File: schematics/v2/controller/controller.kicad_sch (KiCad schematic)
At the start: 68 parts, among them J2 UART, J4 SPI1, J5 Power, J6 Ethernet, J7 Sensors, J8 SPI2, J9 SWD, SW1 BOOT0, SW2 RESET, U1 TPS2120, U2 TPS2120, U4 W5500, U5 AT25SF128A-SHB-T, U6 ADS131M02QPWRQ1, U7 SN74HC153DR, U8 SN74HC74D, U9 STM32G031K6Tx, Y1 KC2520Z, Y2 8.192MHz

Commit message: link controller module: version 1
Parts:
- removed C1, C3: 0.1uF, symbol Device:C_Small
- removed D1: LED, symbol Device:LED
- removed D2: Status, Diode_SMD:D_0603_1608Metric, symbol Device:LED
- removed J2: UART, symbol Connector:Conn_01x03_Pin
- removed J5: Power, symbol Connector:Conn_01x05_Pin
- removed J7: Sensors, symbol Connector:Conn_01x09_Pin
- removed J9: SWD, symbol Connector:Conn_01x05_Pin
- removed JP1: Default Clock Jumper, symbol Jumper:Jumper_3_Bridged12
- removed R10, R13, R4: 5k, symbol Device:R_Small_US
- removed R11: 270, Resistor_SMD:R_0603_1608Metric, symbol Device:R_Small_US
- removed R12, R3: 63.4k, symbol Device:R_Small_US
- removed R14, R5: 51.1K, symbol Device:R_Small_US
- removed R9: 23.7k, symbol Device:R_Small_US
- removed TP1: Vs1, symbol Connector:TestPoint
- removed TP2: Vs2, symbol Connector:TestPoint
- removed U1, U2: TPS2120, Link_Footprints:TPS2120, symbol Link_Components:TPS2120YFPR
- removed U7: SN74HC153DR, D16, symbol Link_Components:SN74HC153D
- removed U8: SN74HC74D, D14, symbol Link_Components:SN74HC74D
- added C22, C23: 10uF, Capacitor_SMD:C_0402_1005Metric, symbol Device:C_Small
- added C24, C25, C26: 0.1u, Capacitor_SMD:C_0402_1005Metric, symbol Device:C_Small
- added D4: LED2, Diode_SMD:D_0603_1608Metric, symbol Device:LED
- added D5: Power, Diode_SMD:D_0603_1608Metric, symbol Device:LED
- added FB2: FerriteBead_Small, Capacitor_SMD:C_0805_2012Metric, symbol Device:FerriteBead_Small
- added J1: Ethernet, Connector_PinHeader_2.54mm:PinHeader_1x06_P2.54mm_Vertical, symbol Connector:Conn_01x06_Pin
- added J3: Conn_ST_STDC14, Link_Footprints:FTSH_107_01_L_DV_K, symbol Connector:Conn_ST_STDC14
- added J8: Power, Connector_PinHeader_2.54mm:PinHeader_1x03_P2.54mm_Vertical, symbol Connector:Conn_01x03_Pin
- added R16, R17: 270, Resistor_SMD:R_0402_1005Metric, symbol Device:R_Small_US
- C1: renamed from C26; footprint (none) -> Capacitor_SMD:C_0402_1005Metric
- C10: renamed from C4; footprint (none) -> Capacitor_SMD:C_0402_1005Metric
- C11: renamed from C5; value 100nF -> 0.1uF; footprint (none) -> Capacitor_SMD:C_0402_1005Metric
- C12: renamed from C6; footprint (none) -> Capacitor_SMD:C_0402_1005Metric
- C13: renamed from C7; footprint (none) -> Capacitor_SMD:C_0402_1005Metric
- C14: renamed from C8; footprint (none) -> Capacitor_SMD:C_0402_1005Metric
- C15: renamed from C9; footprint (none) -> Capacitor_SMD:C_0402_1005Metric
- C16: renamed from C10; footprint (none) -> Capacitor_SMD:C_0402_1005Metric
- C17: renamed from C11; footprint (none) -> Capacitor_SMD:C_0402_1005Metric
- C18: renamed from C12; footprint (none) -> Capacitor_SMD:C_0402_1005Metric
- C19: renamed from C13; footprint (none) -> Capacitor_SMD:C_0402_1005Metric
- C2: renamed from C27; footprint (none) -> Capacitor_SMD:C_0402_1005Metric
- C20: renamed from C14; footprint (none) -> Capacitor_SMD:C_0402_1005Metric
- C21: renamed from C15; footprint (none) -> Capacitor_SMD:C_0402_1005Metric
- C3: renamed from C21; footprint (none) -> Capacitor_SMD:C_0402_1005Metric
- C4: renamed from C22; footprint (none) -> Capacitor_SMD:C_0402_1005Metric
- C5: renamed from C23; footprint (none) -> Capacitor_SMD:C_0402_1005Metric
- C6: renamed from C24; footprint (none) -> Capacitor_SMD:C_0402_1005Metric
- C8: renamed from C25; footprint (none) -> Capacitor_SMD:C_0402_1005Metric
- C9: renamed from C2; value 100n -> 0.1uF; footprint Capacitor_SMD:C_0603_1608Metric -> Capacitor_SMD:C_0402_1005Metric
- D3: value LED -> LED1; footprint (none) -> Diode_SMD:D_0603_1608Metric; LCSC (none) -> C2288; MPN (none) -> KT-0603B
- FB1: footprint (none) -> Capacitor_SMD:C_0805_2012Metric
- J4: footprint (none) -> Connector_PinHeader_2.54mm:PinHeader_1x05_P2.54mm_Vertical
- J5: renamed from J8; footprint (none) -> Connector_PinHeader_2.54mm:PinHeader_1x06_P2.54mm_Vertical
- J6: value Ethernet -> Sensors; footprint (none) -> Connector_PinHeader_2.54mm:PinHeader_1x08_P2.54mm_Vertical
- R1: value 23.7k -> 10k; footprint (none) -> Resistor_SMD:R_0402_1005Metric
- R11: renamed from R6; footprint Resistor_SMD:R_0603_1608Metric -> Resistor_SMD:R_0402_1005Metric
- R12: renamed from R8; footprint Resistor_SMD:R_0603_1608Metric -> Resistor_SMD:R_0402_1005Metric
- R14: renamed from R16; footprint (none) -> Resistor_SMD:R_0402_1005Metric
- R15: footprint (none) -> Resistor_SMD:R_0402_1005Metric; LCSC (none) -> C22369858; MPN (none) -> RCA03270RFLF
- R2: value 5k -> 10k; footprint (none) -> Resistor_SMD:R_0402_1005Metric
- R3: renamed from R17; footprint (none) -> Resistor_SMD:R_0402_1005Metric
- R4: renamed from R18; footprint (none) -> Resistor_SMD:R_0402_1005Metric
- R5: renamed from R20; footprint (none) -> Resistor_SMD:R_0402_1005Metric
- R6: renamed from R19; footprint (none) -> Resistor_SMD:R_0402_1005Metric
- R7: value 270 -> 10k; footprint (none) -> Resistor_SMD:R_0402_1005Metric
- U4: renamed from U6; footprint TSSOP20_PW_TEX -> Link_Footprints:ADS131M02-Q1
- U6: renamed from U5; footprint IC8_AT25SF128A-SHB-T_ADO -> Link_Footprints:AT25SF128A-SHB-T
- renumbered U9 to U5, U4 to U7, Y2 to Y1, Y1 to Y2
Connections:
- net ADS_Clock is gone; now on net PLL_Clock: U4.17 (CLKIN)
- net PS_Sel1 is gone; now on net W5500_NSS: U5.15 (PB0)
- net PS_Sel2 is gone; now on net LED1: U5.16 (PB1)
- net +3V3A: now also FB2.2; no longer FB1.2, U4.1 (AVDD)
- net +3V3D: now also R1.1, R2.1, R7.1, C22.2, C23.1, C24.2, C25.2, C26.2, FB2.1, J3.3 (VCC), J8.1 (Pin_1), J8.3 (Pin_3), R17.1; no longer C3.1, C4.1
- net 8.192MHz: now also U5.2 (PC14)
- net ACTLED: now also J1.6 (Pin_6); no longer J6.8 (Pin_8)
- net GND: now also J6.8 (Pin_8), C22.1, C23.2, C24.1, C25.1, C26.1, D4.1 (K), D5.1 (K), J3.11 (GNDDetect), J3.5 (GND), J3.7 (GND), J8.2 (Pin_2); no longer R2.1
- net LINKLED: now also J1.5 (Pin_5); no longer J6.7 (Pin_7)
- net N_RST: now also J3.12 (~{RST})
- net RX+: now also J1.4 (Pin_4); no longer J6.4 (Pin_4)
- net RX-: now also J1.3 (Pin_3); no longer J6.5 (Pin_5)
- net S1+: now also J6.5 (Pin_5)
- net S1-: now also J6.4 (Pin_4)
- net S2+: now also J6.1 (Pin_1), R6.1; no longer R5.1
- net S2-: now also J6.2 (Pin_2), R5.1; no longer R6.1
- net SDI: now also J6.7 (Pin_7), U5.18 (PA8); no longer U5.3 (PC15)
- net SPI1_MISO: now also U5.22 (PA11[PA9]); no longer U5.13 (PA6)
- net SPI1_MOSI: now also U5.23 (PA12[PA10]); no longer U5.14 (PA7)
- net SPI1_SCK: now also U5.27 (PB3); no longer U5.12 (PA5)
- net SPI2_MISO: now also J5.4 (Pin_4), U5.10 (PA3); no longer J5.3 (Pin_3), U5.30 (PB6)
- net SPI2_MOSI: now also J5.3 (Pin_3), U5.11 (PA4); no longer J5.2 (Pin_2), U5.31 (PB7)
- net SPI2_SCK: now also J5.2 (Pin_2), U5.7 (PA0); no longer J5.4 (Pin_4), U5.32 (PB8)
- net SWDIO: now also J3.4 (JTMS/SWDIO)
- net TX+: now also J1.2 (Pin_2); no longer J6.1 (Pin_1)
- net TX-: now also J1.1 (Pin_1); no longer J6.2 (Pin_2)
- net UART_RX: now also U5.31 (PB7), J3.13 (VCP_RX); no longer U5.10 (PA3)
- net UART_TX: now also U5.30 (PB6), J3.14 (VCP_TX); no longer U5.9 (PA2)
- net W5500_INTn: now also U5.13 (PA6); no longer U5.17 (PB2)
- net W5500_RST: now also U5.12 (PA5); no longer U5.27 (PB3)
- net MEM_NSS: now reaches R2.2
- net MEM_NSS: now also J5.6 (Pin_6), U5.14 (PA7), U6.1 (CS); no longer R1.1
- net LED1: now reaches R15.1
- net W5500_NSS: now reaches R7.2
- net W5500_NSS: now also J5.5 (Pin_5), U7.32 (~{SCS})
- net PLL_Clock: now reaches U5.19 (PA9)
- net +5V renamed ADC_NSS
- net ADC_NSS: now also J4.5 (Pin_5), U4.12 (CS), U5.26 (PA15)
- net ADS_ClockSelA renamed ADC_DRDY
- net ADC_DRDY: now also U4.13 (DRDY)
- net ADS_ClockSelB renamed ADC_RST
- net ADC_RST: now also U4.11 (*SYNC/RESET)
- removed net ADS_DRDY: U4.13 (DRDY), U5.26 (PA15)
- removed net ADS_RST: U4.11 (*SYNC/RESET), U5.23 (PA10/PA12)
- net BOOT0/SWCLK renamed BOOT0
- net BOOT0: now also J3.6 (JCLK/SWCLK)
- removed net SPI1_CS: J4.5 (Pin_5), U4.12 (CS), U5.11 (PA4)
- removed net SPI2_CS1: J5.6 (Pin_6), U5.18 (PA8), U7.32 (~{SCS})
- removed net SPI2_CS2: J5.5 (Pin_5), U5.22 (PA9/PA11), U6.1 (CS)
- net STATUS: no longer names the net of U5.8 (PA1)
- new net: D5.2 (A), R17.2
- new net: D4.2 (A), R16.2
- new net +3V3A1: C3.1, C4.1, FB1.2, U4.1 (AVDD)
- new net LED2: R16.1, U5.17 (PB2)
- no-connect marks 26 -> 24
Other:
- note removed: "PS Select 1"
- note removed: "PS Select 2"
- note removed: "SWD"
- note removed: "UART"
- moved on the sheet: C10, C11, C5, C6, C9, J4, J5, R11, R12, SW1, SW2, Y1

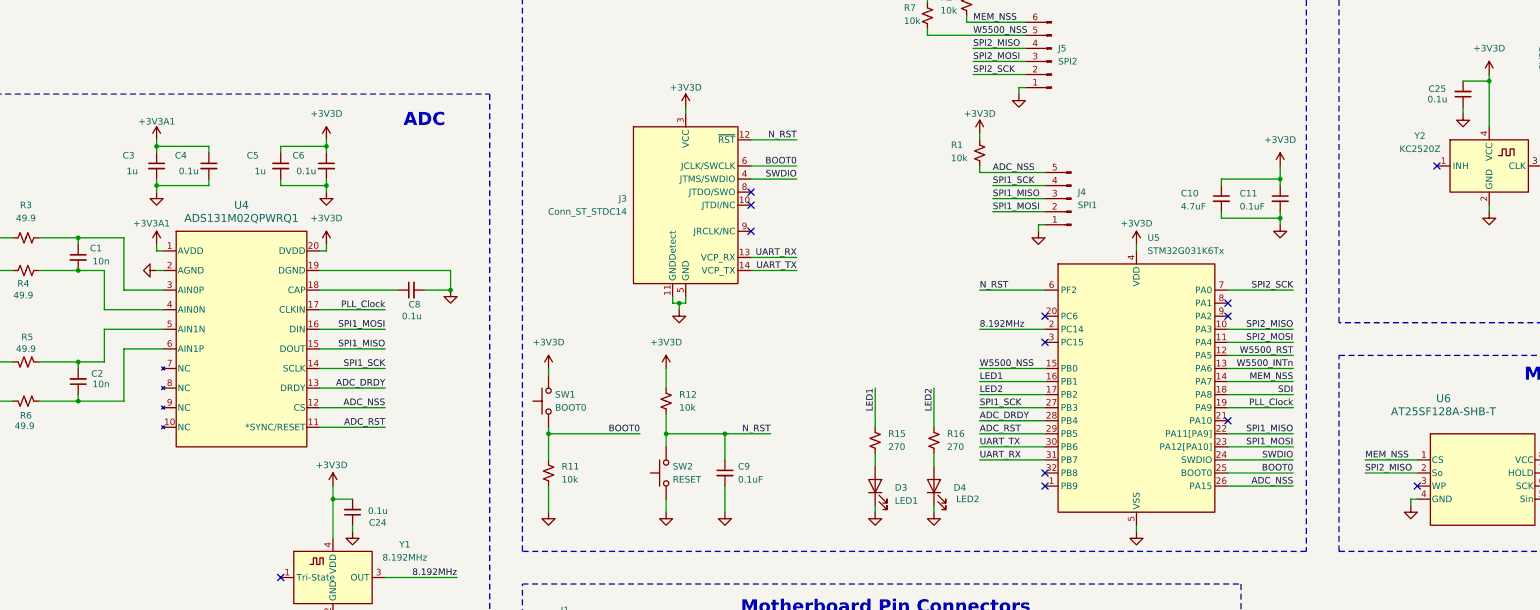
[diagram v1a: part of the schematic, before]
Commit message: fix(controller): component calue comments
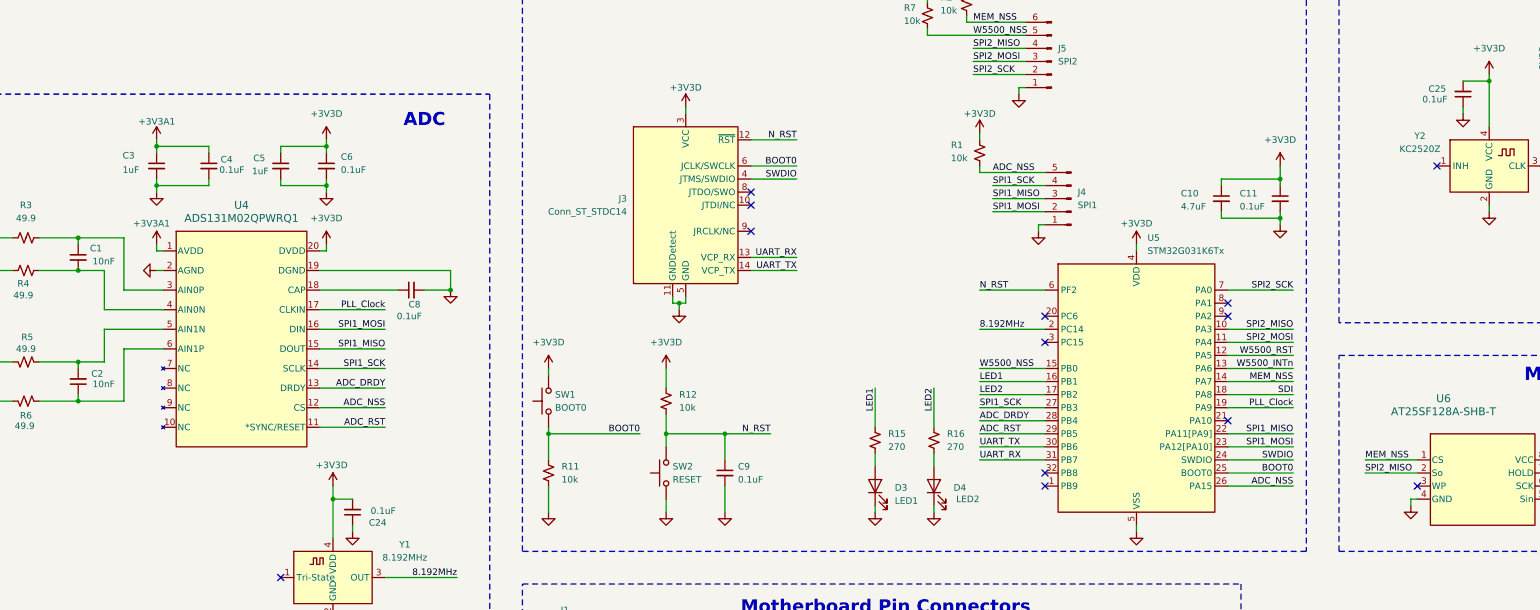
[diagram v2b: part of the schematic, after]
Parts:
- C1, C2: value 10n -> 10nF
- C24, C25, C4, C6, C8: value 0.1u -> 0.1uF
- C3, C5: value 1u -> 1uF
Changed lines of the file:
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@@
 			)
 		)
-		(property "Value" "1u"
-			(at 50.038 110.236 0)
+		(property "Value" "1uF"
+			(at 49.276 109.982 0)
 			(effects
 				(font
@@
 		(dnp no)
 		(property "Reference" "C5"
-			(at 73.406 107.188 0)
+			(at 74.676 107.696 0)
 			(effects
 				(font
@@
 			)
 		)
-		(property "Value" "1u"
-			(at 74.93 110.236 0)
+		(property "Value" "1uF"
+			(at 74.422 110.236 0)
 			(effects
 				(font
@@
 			)
 		)
-		(property "Value" "10n"
+		(property "Value" "10nF"
 			(at 43.434 127.762 0)
 			(effects
@@
 		(dnp no)
 		(property "Reference" "C6"
-			(at 82.296 107.188 0)
+			(at 91.694 107.442 0)
 			(effects
 				(font
@@
 			)
 		)
-		(property "Value" "0.1u"
-			(at 83.058 110.236 0)
+		(property "Value" "0.1uF"
+			(at 91.694 109.982 0)
 			(effects
 				(font
@@
 			)
 		)
-		(property "Value" "0.1u"
-			(at 100.838 176.276 0)
+		(property "Value" "0.1uF"
+			(at 102.362 176.276 0)
 			(effects
 				(font
@@
 		(dnp no)
 		(property "Reference" "C4"
-			(at 59.436 107.188 0)
+			(at 68.326 107.95 0)
 			(effects
 				(font
@@
 			)
 		)
-		(property "Value" "0.1u"
-			(at 60.198 110.236 0)
+		(property "Value" "0.1uF"
+			(at 68.072 109.982 0)
 			(effects
 				(font
@@
 			)
 		)
-		(property "Value" "0.1u"
+		(property "Value" "0.1uF"
 			(at 107.442 138.43 90)
 			(effects
@@
 			)
 		)
-		(property "Value" "10n"
+		(property "Value" "10nF"
 			(at 43.434 151.638 0)
 			(effects
@@
 			)
 		)
-		(property "Value" "0.1u"
+		(property "Value" "0.1uF"
 			(at 306.832 96.266 0)
 			(effects
